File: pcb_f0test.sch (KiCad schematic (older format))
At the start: 36 parts, among them P1 CONN_02X04, P2 CONN_01X02, U1 STM32F042GxU, U2 LP2985LV

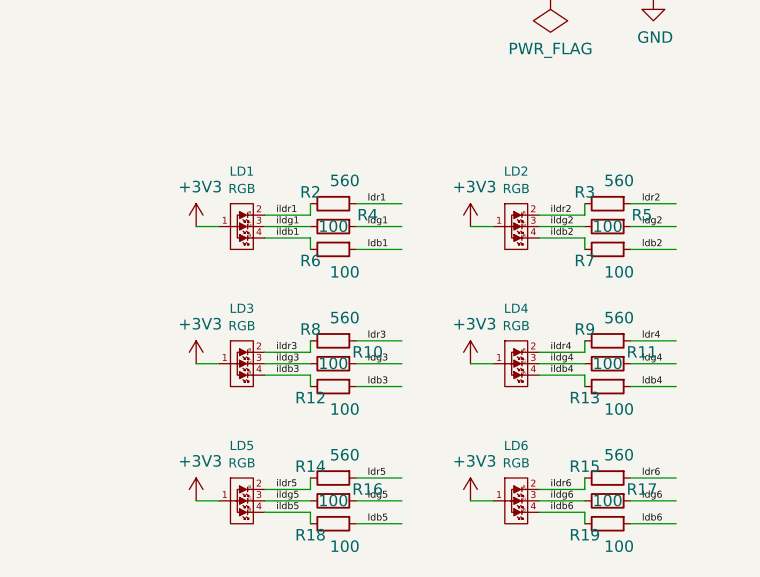
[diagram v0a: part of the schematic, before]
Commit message: Fix numbering of LEDs.
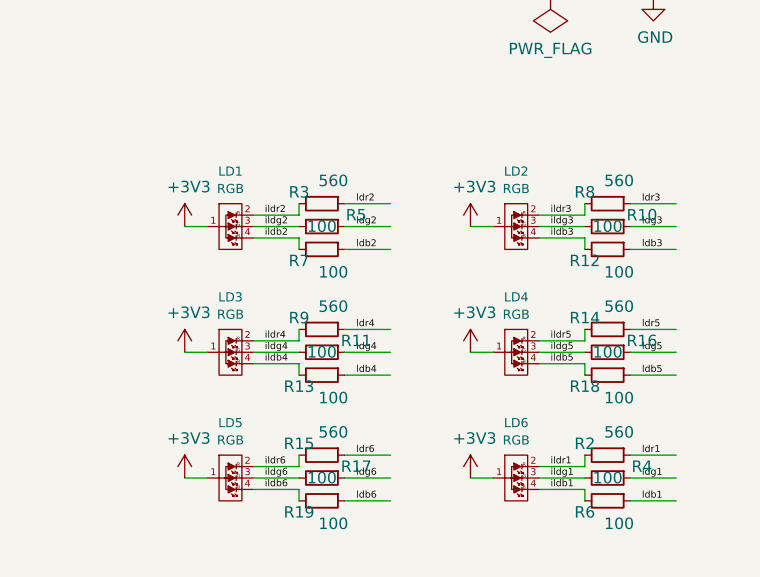
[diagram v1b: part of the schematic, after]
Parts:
- U1: footprint knielsenlib:UFQFPN28 -> knielsenlib:UFQFPN28_fixpad
- renumbered LD2 to LD1, LD3 to LD2, LD4 to LD3, LD5 to LD4, LD6 to LD5, LD1 to LD6
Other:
- moved on the sheet: LD1, LD2, LD3, LD4, LD5, LD6, R10, R11, R12, R13, R14, R15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

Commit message: Add pogopin board, fixing pogopad layout.
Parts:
- removed P1: CONN_02X04, knielsenlib:TestPoints2x4, symbol CONN_02X04
- added P6: CONN_02X05, knielsenlib:pogopads_2x5_50mil_smd, symbol CONN_02X05
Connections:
- wire segments 116 -> 119
- no-connect marks 0 -> 1
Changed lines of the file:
@@
 $Descr A4 11693 8268
 encoding utf-8
-Sheet 1 1
+Sheet 1 2
 Title ""
 Date ""
@@
 Text Label 1750 3100 0    60   ~ 0
 nrst
-$Comp
-L CONN_02X04 P1
-U 1 1 57540C3E
-P 2400 4550
-F 0 "P1" H 2400 4915 50  0000 C CNN
-F 1 "CONN_02X04" H 2400 4824 50  0000 C CNN
-F 2 "knielsenlib:TestPoints2x4" H 2400 3350 50  0001 C CNN
-F 3 "" H 2400 3350 50  0000 C CNN
-	1    2400 4550
-	1    0    0    -1
-$EndComp
-Wire Wire Line
-	2150 4400 1650 4400
-Wire Wire Line
-	2150 4500 1650 4500
-Wire Wire Line
-	2150 4600 1650 4600
-Wire Wire Line
-	2150 4700 1650 4700
-Wire Wire Line
-	3150 4400 2650 4400
-Wire Wire Line
-	3150 4500 2650 4500
-Wire Wire Line
-	3150 4600 2650 4600
-Wire Wire Line
-	3150 4700 2650 4700
-$Comp
-L +3V3 #PWR08
-U 1 1 57540D54
-P 3150 4700
-F 0 "#PWR08" H 3150 4550 50  0001 C CNN
-F 1 "+3V3" H 3168 4873 50  0000 C CNN
-F 2 "" H 3150 4700 50  0000 C CNN
-F 3 "" H 3150 4700 50  0000 C CNN
-	1    3150 4700
-	-1   0    0    1
-$EndComp
-$Comp
-L GND #PWR09
-U 1 1 57540DCD
-P 1650 4800
-F 0 "#PWR09" H 1650 4550 50  0001 C CNN
-F 1 "GND" H 1658 4627 50  0000 C CNN
-F 2 "" H 1650 4800 50  0000 C CNN
-F 3 "" H 1650 4800 50  0000 C CNN
-	1    1650 4800
-	1    0    0    -1
-$EndComp
-Text Label 1800 4500 0    60   ~ 0
-usb_dm
-Text Label 2700 4600 0    60   ~ 0
-boot0
-Text Label 1800 4600 0    60   ~ 0
-nrst
-Text Label 2700 4400 0    60   ~ 0
-swclk
-Text Label 2700 4500 0    60   ~ 0
-usb_dp
-Text Label 1800 4400 0    60   ~ 0
-swdio
 Wire Wire Line
 	2100 2500 1650 2500
@@
 	4450 4500 4450 4400
 $Comp
-L VCC #PWR010
+L VCC #PWR08
 U 1 1 57541920
 P 4450 4400
-F 0 "#PWR010" H 4450 4250 50  0001 C CNN
+F 0 "#PWR08" H 4450 4250 50  0001 C CNN
 F 1 "VCC" H 4470 4573 50  0000 C CNN
 F 2 "" H 4450 4400 50  0000 C CNN
@@
 	4450 4600 4450 4700
 $Comp
-L GND #PWR011
+L GND #PWR09
 U 1 1 5754198E
 P 4450 4700
-F 0 "#PWR011" H 4450 4450 50  0001 C CNN
+F 0 "#PWR09" H 4450 4450 50  0001 C CNN
 F 1 "GND" H 4458 4527 50  0000 C CNN
 F 2 "" H 4450 4700 50  0000 C CNN
@@
 Connection ~ 4450 4500
 $Comp
-L PWR_FLAG #FLG012
+L PWR_FLAG #FLG010
 U 1 1 57541A2B
 P 4600 4400
-F 0 "#FLG012" H 4600 4495 50  0001 C CNN
+F 0 "#FLG010" H 4600 4495 50  0001 C CNN
 F 1 "PWR_FLAG" V 4600 4578 50  0000 L CNN
 F 2 "" H 4600 4400 50  0000 C CNN
@@
 	7200 5000 7300 5000
 $Comp
-L +3V3 #PWR013
+L +3V3 #PWR011
 U 1 1 57548B3B
 P 7200 5000
-F 0 "#PWR013" H 7200 4850 50  0001 C CNN
+F 0 "#PWR011" H 7200 4850 50  0001 C CNN
 F 1 "+3V3" H 7218 5173 50  0000 C CNN
 F 2 "" H 7200 5000 50  0000 C CNN
@@
 	5950 3900 6050 3900
 $Comp
-L +3V3 #PWR014
+L +3V3 #PWR012
 U 1 1 5754991A
 P 5950 3900
-F 0 "#PWR014" H 5950 3750 50  0001 C CNN
+F 0 "#PWR012" H 5950 3750 50  0001 C CNN
 F 1 "+3V3" H 5968 4073 50  0000 C CNN
 F 2 "" H 5950 3900 50  0000 C CNN
@@
 	7200 3900 7300 3900
 $Comp
-L +3V3 #PWR015
+L +3V3 #PWR013
 U 1 1 57549EC0
 P 7200 3900
-F 0 "#PWR015" H 7200 3750 50  0001 C CNN
+F 0 "#PWR013" H 7200 3750 50  0001 C CNN
 F 1 "+3V3" H 7218 4073 50  0000 C CNN
 F 2 "" H 7200 3900 50  0000 C CNN
@@
 	5950 4450 6050 4450
 $Comp
-L +3V3 #PWR016
+L +3V3 #PWR014
 U 1 1 57549EF1
 P 5950 4450
-F 0 "#PWR016" H 5950 4300 50  0001 C CNN
+F 0 "#PWR014" H 5950 4300 50  0001 C CNN
 F 1 "+3V3" H 5968 4623 50  0000 C CNN
 F 2 "" H 5950 4450 50  0000 C CNN
@@
 	7200 4450 7300 4450
 $Comp
-L +3V3 #PWR017
+L +3V3 #PWR015
 U 1 1 5754A27E
 P 7200 4450
-F 0 "#PWR017" H 7200 4300 50  0001 C CNN
+F 0 "#PWR015" H 7200 4300 50  0001 C CNN
 F 1 "+3V3" H 7218 4623 50  0000 C CNN
 F 2 "" H 7200 4450 50  0000 C CNN
@@
 	5950 5000 6050 5000
 $Comp
-L +3V3 #PWR018
+L +3V3 #PWR016
 U 1 1 5754A2AF
 P 5950 5000
-F 0 "#PWR018" H 5950 4850 50  0001 C CNN
+F 0 "#PWR016" H 5950 4850 50  0001 C CNN
 F 1 "+3V3" H 5968 5173 50  0000 C CNN
 F 2 "" H 5950 5000 50  0000 C CNN
@@
 Text Label 3600 1800 0    60   ~ 0
 ldb6
-Wire Wire Line
-	1650 4700 1650 4800
+$Sheet
+S 8900 1050 1550 1150
+U 576F9AE1
+F0 "sheet_pogopins" 60
+F1 "sheet_pogopins.sch" 60
+$EndSheet
+Wire Wire Line
+	2300 4650 1800 4650
+Text Label 2850 4350 0    60   ~ 0
+boot0
+Text Label 1950 4250 0    60   ~ 0
+usb_dp
+Text Label 1950 4450 0    60   ~ 0
+swclk
+Text Label 2850 4450 0    60   ~ 0
+nrst
+Text Label 2850 4250 0    60   ~ 0
+usb_dm
+Text Label 1950 4350 0    60   ~ 0
+swdio
+Wire Wire Line
+	1800 4650 1800 4750
+$Comp
+L GND #PWR017
+U 1 1 576FB426
+P 1800 4750
+F 0 "#PWR017" H 1800 4500 50  0001 C CNN
+F 1 "GND" H 1808 4577 50  0000 C CNN
+F 2 "" H 1800 4750 50  0000 C CNN
+F 3 "" H 1800 4750 50  0000 C CNN
+	1    1800 4750
+	-1   0    0    -1
+$EndComp
+$Comp
+L VCC #PWR018
+U 1 1 576FB53C
+P 1800 4500
+F 0 "#PWR018" H 1800 4350 50  0001 C CNN
+F 1 "VCC" H 1820 4673 50  0000 C CNN
+F 2 "" H 1800 4500 50  0000 C CNN
+F 3 "" H 1800 4500 50  0000 C CNN
+	1    1800 4500
+	1    0    0    -1
+$EndComp
+$Comp
+L +3V3 #PWR019
+U 1 1 576FB652
+P 3400 4500
+F 0 "#PWR019" H 3400 4350 50  0001 C CNN
+F 1 "+3V3" H 3418 4673 50  0000 C CNN
+F 2 "" H 3400 4500 50  0000 C CNN
+F 3 "" H 3400 4500 50  0000 C CNN
+	1    3400 4500
+	1    0    0    -1
+$EndComp
+$Comp
+L CONN_02X05 P6
+U 1 1 5772A77B
+P 2550 4450
+F 0 "P6" H 2550 4019 50  0000 C CNN
+F 1 "CONN_02X05" H 2550 4110 50  0000 C CNN
+F 2 "knielsenlib:pogopads_2x5_50mil_smd" H 2550 3250 50  0001 C CNN
+F 3 "" H 2550 3250 50  0000 C CNN
+	1    2550 4450
+	1    0    0    1
+$EndComp
+NoConn ~ 2800 4650
+Wire Wire Line
+	2300 4550 1800 4550
+Wire Wire Line
+	1800 4550 1800 4500
+Wire Wire Line
+	2800 4550 3400 4550
+Wire Wire Line
+	3400 4550 3400 4500
+Wire Wire Line
+	2300 4250 1900 4250
+Wire Wire Line
+	2300 4350 1900 4350
+Wire Wire Line
+	2300 4450 1900 4450
+Wire Wire Line
+	2800 4250 3250 4250
+Wire Wire Line
+	2800 4350 3250 4350
+Wire Wire Line
+	2800 4450 3250 4450
 $EndSCHEMATC

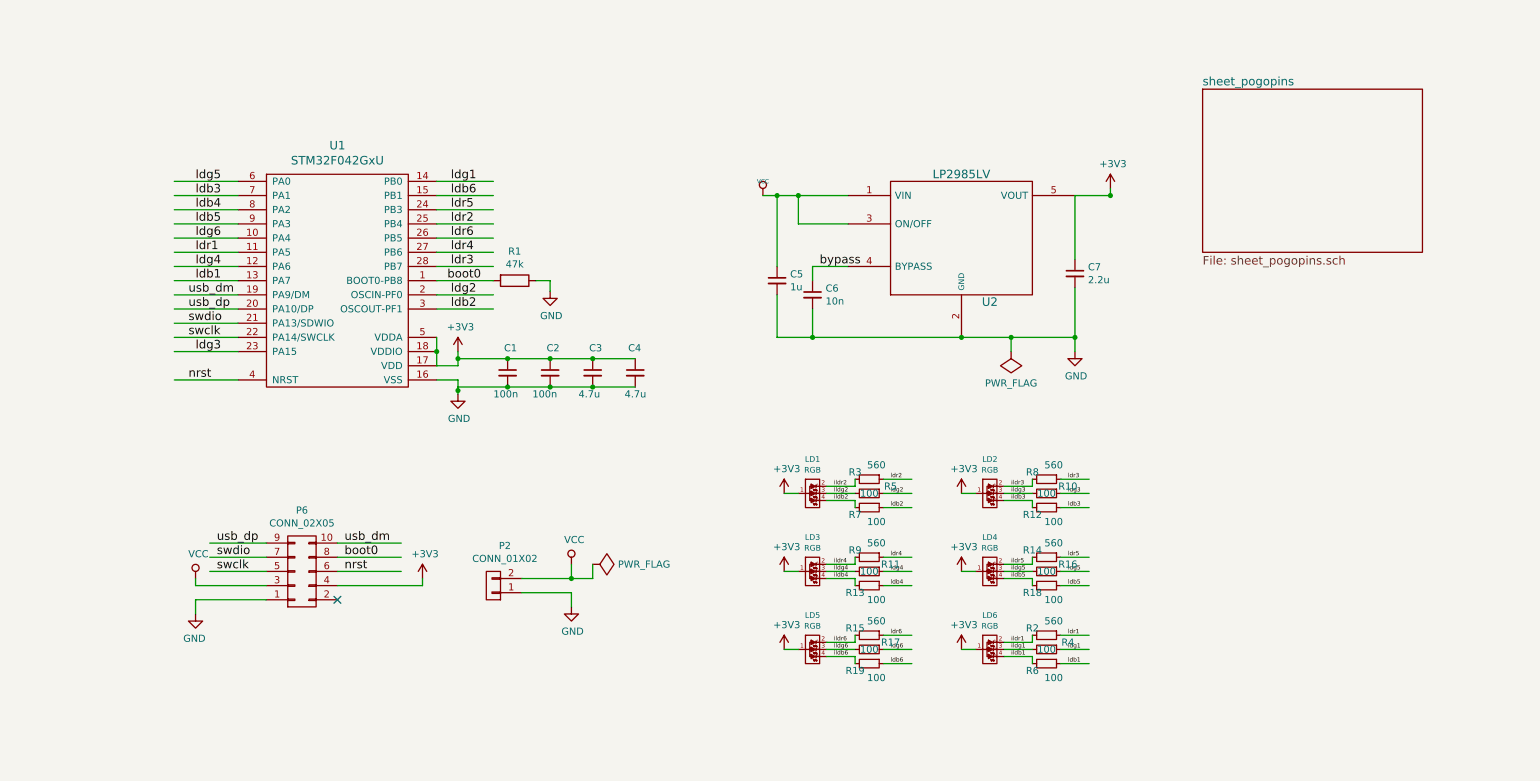
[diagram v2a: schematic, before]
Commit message: Initial stab at a "christmas heart" decoration pcb.
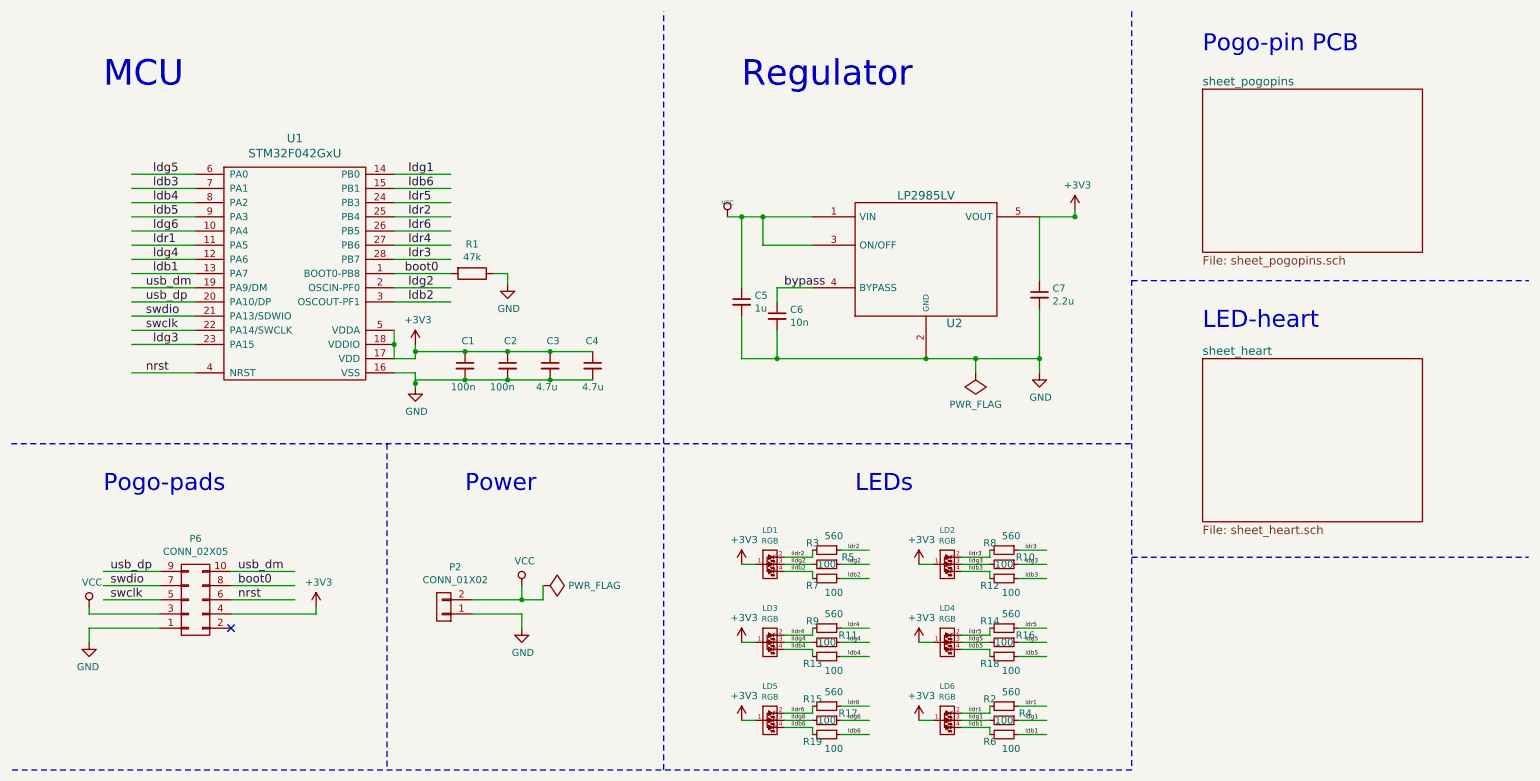
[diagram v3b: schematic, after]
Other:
- note added: "LED-heart"
- note added: "LEDs"
- note added: "MCU"
- note added: "Pogo-pads"
- note added: "Pogo-pin PCB"
- note added: "Power"
- note added: "Regulator"
- moved on the sheet: C1, C2, C3, C4, C5, C6, C7, LD1, LD2, LD3, LD4, LD5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
